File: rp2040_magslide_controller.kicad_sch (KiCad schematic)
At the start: 1 part

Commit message: Inc
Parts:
- added C? (x12): (no value), symbol Device:C_Small
- added C?: 0.1u, symbol Device:C_Small
- added C? (x2): 4u7, Capacitor_SMD:C_0603_1608Metric, symbol Device:C_Small
- added C? (x2): 1u, Capacitor_SMD:C_0603_1608Metric, symbol Device:C_Small
- added C? (x2): 100n, Capacitor_SMD:C_0402_1005Metric, symbol Device:C_Small
- added J? (x2): Conn_01x20_Female, misc:20_pin_header, symbol Connector:Conn_01x20_Female
- added J?: USB_B_Mini, Connector_USB:USB_Micro-B_Molex-105017-0001, symbol Connector:USB_B_Mini
- added J?: 50-00174, misc:54-00174, symbol misc:50-00174
- added J?: Conn_02x05_Odd_Even, Connector:Tag-Connect_TC2050-IDC-NL_2x05_P1.27mm_Vertical, symbol Connector_Generic:Conn_02x05_Odd_Even
- added JP? (x2): SolderJumper_2_Open, Jumper:SolderJumper-2_P1.3mm_Open_TrianglePad1.0x1.5mm, symbol Jumper:SolderJumper_2_Open
- added R? (x3): (no value), symbol Device:R_Small
- added R? (x2): 10k, Resistor_SMD:R_0402_1005Metric, symbol Device:R_Small
- added R? (x4): 4.7k, Resistor_SMD:R_0402_1005Metric, symbol Device:R_Small
- added R?: 27R 0603, symbol Device:R_Small
- added R?: 1K, symbol Device:R_Small
- added SW?: (no value), symbol Switch:SW_SPST
- added SW?: SW_SPST, symbol Switch:SW_SPST
- added U? (x2): CD74HC4067SM, Package_SO:SSOP-24_5.3x8.2mm_P0.65mm, symbol 74xx:CD74HC4067SM
- added U?: (no value), symbol Memory_Flash_Extra:W25Q64JV
- added U?: AMS1117-3.3, Package_TO_SOT_SMD:SOT-223-3_TabPin2, symbol Regulator_Linear:AMS1117-3.3
- added Y?: (no value), symbol Device:Crystal_GND24_Small
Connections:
- net +3V3: now reaches U?.1 (IOVDD)
- net +3V3: now also U?.10 (IOVDD), U?.22 (IOVDD), U?.33 (IOVDD), U?.42 (IOVDD), U?.43 (ADC_AVDD), U?.44 (VREG_IN), U?.48 (USB_VDD), U?.49 (IOVDD), C?.1, C?.1, C?.1, C?.1, C?.1, C?.2, C?.2, C?.2, C?.2, C?.2, C?.2, C?.2, J?.1 (Pin_1), J?.1 (Pin_1), J?.15 (Pin_15), J?.2 (Pin_2), J?.8 (Pin_8), J?.9 (Pin_9), R?.1, R?.1, R?.1, R?.1, R?.1, R?.2, U?.2 (VO), U?.24 (VCC), U?.24 (VCC), U?.8 (VDD)
- net MUX_01: now reaches U?.11 (GPIO8)
- net MUX_01: now also U?.11 (S1)
- net MUX_02: now reaches U?.12 (GPIO9)
- net MUX_02: now also U?.14 (S2)
- net MUX_03: now reaches U?.13 (GPIO10)
- net MUX_03: now also U?.13 (S3)
- net MUX1_EN: now reaches U?.14 (GPIO11)
- net MUX1_EN: now also R?.1, U?.15 (~{E})
- net MUX_10: now reaches U?.15 (GPIO12)
- net MUX_10: now also U?.10 (S0)
- net MUX_11: now reaches U?.16 (GPIO13)
- net MUX_11: now also U?.11 (S1)
- net MUX_12: now reaches U?.17 (GPIO14)
- net MUX_12: now also U?.14 (S2)
- net MUX_13: now reaches U?.18 (GPIO15)
- net MUX_13: now also U?.13 (S3)
- net GND: now reaches U?.19 (TESTEN)
- net GND: now also U?.57 (GND), C?.1, C?.1, C?.1, C?.1, C?.1, C?.1, C?.1, C?.1, C?.1, C?.1, C?.1, C?.1, C?.2, C?.2, C?.2, C?.2, C?.2, C?.2, C?.2, J?.10 (Pin_10), J?.16 (Pin_16), J?.19 (Pin_19), J?.2 (Pin_2), J?.3 (Pin_3), J?.3 (Pin_3), J?.4, J?.5 (GND), J?.5 (Pin_5), J?.6 (Shield), J?.9 (Pin_9), J?.9 (Pin_9), R?.2, R?.2, SW?.1 (A), SW?.1 (A), U?.1 (GND), U?.12 (GND), U?.12 (GND), U?.4 (GND), U?.9 (GND), Y?.2, Y?.4
- net dbg_tx: now reaches U?.2 (GPIO0)
- net dbg_tx: now also J?.8 (Pin_8)
- net at U?.20 (XIN): now also C?.2, Y?.3
- net at U?.21 (XOUT): now also C?.2, Y?.1
- net at U?.23 (DVDD): now also C?.2
- net SWCLK: now reaches U?.24 (SWCLK)
- net SWCLK: now also J?.4 (Pin_4)
- net SWDIO: now reaches U?.25 (SWD)
- net SWDIO: now also J?.2 (Pin_2)
- net at U?.26 (RUN): now also R?.2, SW?.2 (B)
- net dbg_rx: now reaches U?.3 (GPIO1)
- net dbg_rx: now also J?.6 (Pin_6)
- net ADC_0: now reaches U?.38 (GPIO26_ADC0)
- net ADC_0: now also U?.1 (COM)
- net ADC_1: now reaches U?.39 (GPIO27_ADC1)
- net ADC_1: now also U?.1 (COM)
- net extern_sda: now reaches U?.4 (GPIO2)
- net extern_sda: now also J?.17 (Pin_17), R?.2
- net at U?.45 (VREG_VOUT): now also C?.2
- net at U?.46 (USB_DM): now also R?.1
- net at U?.47 (USB_DP): now also R?.1
- net extern_scl: now reaches U?.5 (GPIO3)
- net extern_scl: now also J?.16 (Pin_16), R?.2
- net at U?.50 (DVDD): now also C?.2
- net QSPI_SD3: now reaches U?.51 (QSPI_SD3)
- net QSPI_SD3: now also U?.7 (~{HOLD}/IO3)
- net QSPI_SCLK: now reaches U?.52 (QSPI_SCLK)
- net QSPI_SCLK: now also U?.6 (SCK)
- net QSPI_SD0: now reaches U?.53 (QSPI_SD0)
- net QSPI_SD0: now also U?.5 (DI/IO0)
- net QSPI_SD2: now reaches U?.54 (QSPI_SD2)
- net QSPI_SD2: now also U?.3 (~{WP}/IO2)
- net QSPI_SD1: now reaches U?.55 (QSPI_SD1)
- net QSPI_SD1: now also U?.2 (DO/IO1)
- net QSPI_CS: now reaches U?.56 (QSPI_SS)
- net QSPI_CS: now also R?.1, R?.2, U?.1 (~{CS})
- net board_sda: now reaches U?.6 (GPIO4)
- net board_sda: now also J?.3, JP?.2 (B)
- net board_scl: now reaches U?.7 (GPIO5)
- net board_scl: now also J?.2, JP?.2 (B)
- net MUX0_EN: now reaches U?.8 (GPIO6)
- net MUX0_EN: now also R?.1, U?.15 (~{E})
- net MUX_00: now reaches U?.9 (GPIO7)
- net MUX_00: now also U?.10 (S0)
- new net: R?.1, SW?.2 (B)
- new net: JP?.1 (A), R?.2 (x2)
- new net +5V: C?.1, C?.1, J?.1, J?.1 (VBUS), J?.18 (Pin_18), U?.3 (VI)
- new net D+: J?.3 (D+), R?.2
- new net D-: J?.2 (D-), R?.2
- new net F00: J?.3 (Pin_3), U?.9 (I0)
- new net F01: J?.4 (Pin_4), U?.8 (I1)
- new net F02: J?.5 (Pin_5), U?.7 (I2)
- new net F03: J?.6 (Pin_6), U?.6 (I3)
- new net F04: J?.7 (Pin_7), U?.5 (I4)
- new net F10: J?.10 (Pin_10), U?.4 (I5)
- new net F11: J?.11 (Pin_11), U?.3 (I6)
- new net F12: J?.12 (Pin_12), U?.2 (I7)
- new net F13: J?.13 (Pin_13), U?.23 (I8)
- new net F14: J?.14 (Pin_14), U?.22 (I9)
- new net F20: J?.17 (Pin_17), U?.21 (I10)
- new net F21: J?.18 (Pin_18), U?.20 (I11)
- new net F22: J?.19 (Pin_19), U?.19 (I12)
- new net F23: J?.20 (Pin_20), U?.18 (I13)
- new net F24: J?.1 (Pin_1), U?.17 (I14)
- new net F30: J?.4 (Pin_4), U?.16 (I15)
- new net F31: J?.5 (Pin_5), U?.9 (I0)
- new net F32: J?.6 (Pin_6), U?.8 (I1)
- new net F33: J?.7 (Pin_7), U?.7 (I2)
- new net F34: J?.8 (Pin_8), U?.6 (I3)
- new net F40: J?.11 (Pin_11), U?.5 (I4)
- new net F41: J?.12 (Pin_12), U?.4 (I5)
- new net F42: J?.13 (Pin_13), U?.3 (I6)
- new net F43: J?.14 (Pin_14), U?.2 (I7)
- new net F44: J?.15 (Pin_15), U?.23 (I8)
- new net SWO: J?.20 (Pin_20)
- no-connect marks 0 -> 22
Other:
- moved on the sheet: U?

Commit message: Inc
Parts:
- gave numbers to parts that had none: 45
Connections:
- net SWO: no longer names the net of J5.20 (Pin_20)
- no-connect marks 22 -> 23

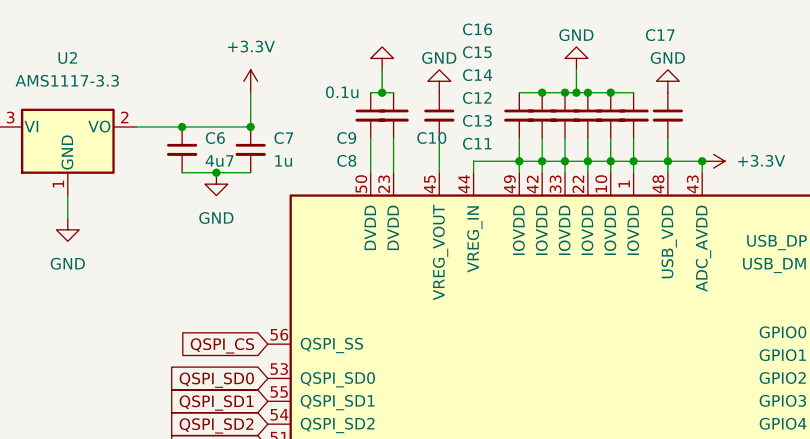
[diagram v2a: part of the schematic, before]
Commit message: DRC pass, next up _review_
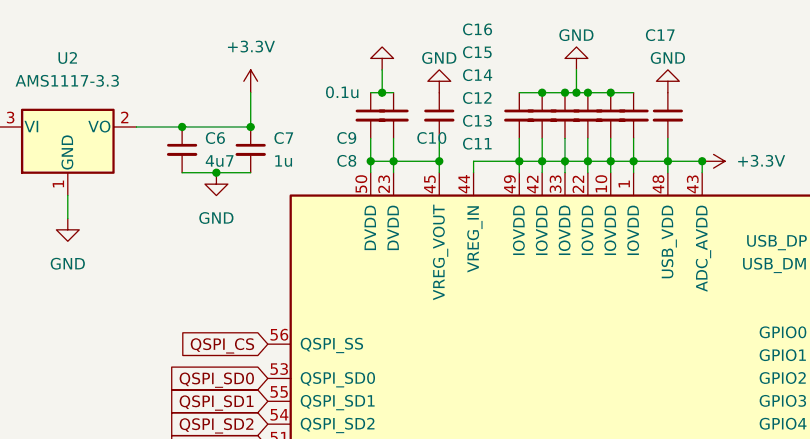
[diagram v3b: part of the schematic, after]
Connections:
- net at C8.2, U3.50 (DVDD): now also C10.2, C9.2, U3.23 (DVDD), U3.45 (VREG_VOUT)
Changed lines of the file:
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@@
   (junction (at 127 20.32) (diameter 0) (color 0 0 0 0)
   )
+  (junction (at 107.95 27.94) (diameter 0) (color 0 0 0 0)
+  )
   (junction (at 47.625 29.21) (diameter 0) (color 0 0 0 0)
   )
+  (junction (at 100.33 27.94) (diameter 0) (color 0 0 0 0)
+  )
   (junction (at 119.38 20.32) (diameter 0) (color 0 0 0 0)
   )
@@
   )
   (junction (at 68.58 87.63) (diameter 0) (color 0 0 0 0)
+  )
+  (junction (at 102.87 27.94) (diameter 0) (color 0 0 0 0)
   )
   (junction (at 137.16 27.94) (diameter 0) (color 0 0 0 0)
@@
     (stroke (width 0) (type default) (color 0 0 0 0))
   )
+  (wire (pts (xy 102.87 27.94) (xy 102.87 29.21))
+    (stroke (width 0) (type default) (color 0 0 0 0))
+  )
+  (wire (pts (xy 100.33 27.94) (xy 102.87 27.94))
+    (stroke (width 0) (type default) (color 0 0 0 0))
+  )
   (wire (pts (xy 79.375 29.21) (xy 83.185 29.21))
     (stroke (width 0) (type default) (color 0 0 0 0))
@@
     (stroke (width 0) (type default) (color 0 0 0 0))
   )
-  (wire (pts (xy 102.87 25.4) (xy 102.87 29.21))
+  (wire (pts (xy 102.87 25.4) (xy 102.87 27.94))
     (stroke (width 0) (type default) (color 0 0 0 0))
   )
@@
     (stroke (width 0) (type default) (color 0 0 0 0))
   )
-  (wire (pts (xy 100.33 25.4) (xy 100.33 29.21))
+  (wire (pts (xy 100.33 25.4) (xy 100.33 27.94))
+    (stroke (width 0) (type default) (color 0 0 0 0))
+  )
+  (wire (pts (xy 100.33 27.94) (xy 100.33 29.21))
     (stroke (width 0) (type default) (color 0 0 0 0))
   )
@@
     (stroke (width 0) (type default) (color 0 0 0 0))
   )
+  (wire (pts (xy 102.87 27.94) (xy 107.95 27.94))
+    (stroke (width 0) (type default) (color 0 0 0 0))
+  )
   (wire (pts (xy 99.695 156.21) (xy 99.695 153.67))
     (stroke (width 0) (type default) (color 0 0 0 0))
@@
     (stroke (width 0) (type default) (color 0 0 0 0))
   )
-  (wire (pts (xy 107.95 25.4) (xy 107.95 29.21))
+  (wire (pts (xy 107.95 25.4) (xy 107.95 27.94))
     (stroke (width 0) (type default) (color 0 0 0 0))
   )
@@
   )
   (wire (pts (xy 35.56 58.42) (xy 35.56 57.15))
+    (stroke (width 0) (type default) (color 0 0 0 0))
+  )
+  (wire (pts (xy 107.95 27.94) (xy 107.95 29.21))
     (stroke (width 0) (type default) (color 0 0 0 0))
   )
@@
       (effects (font (size 1.27 1.27)) (justify left))
     )
-    (property "Value" "" (id 1) (at 107.95 25.4 0)
+    (property "Value" "" (id 1) (at 104.775 20.32 0)
       (effects (font (size 1.27 1.27)) (justify left))
     )
